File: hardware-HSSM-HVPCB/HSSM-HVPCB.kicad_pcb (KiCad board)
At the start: 2 copper layers, 42 x 36 mm, 66 parts, among them J1 2086-1103, J2 2601-1110, K1 G6DN-1A-L DC12, K2 G6DN-1A-L DC12, Q1 Q_NMOS_SOT-23_IRLML6344, Q2 Q_NMOS_SOT-23_IRLML6344, U1 LNK3204D-TL, U2 CS5480-INZ, U3 LTV-354T, U4 LTV-354T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

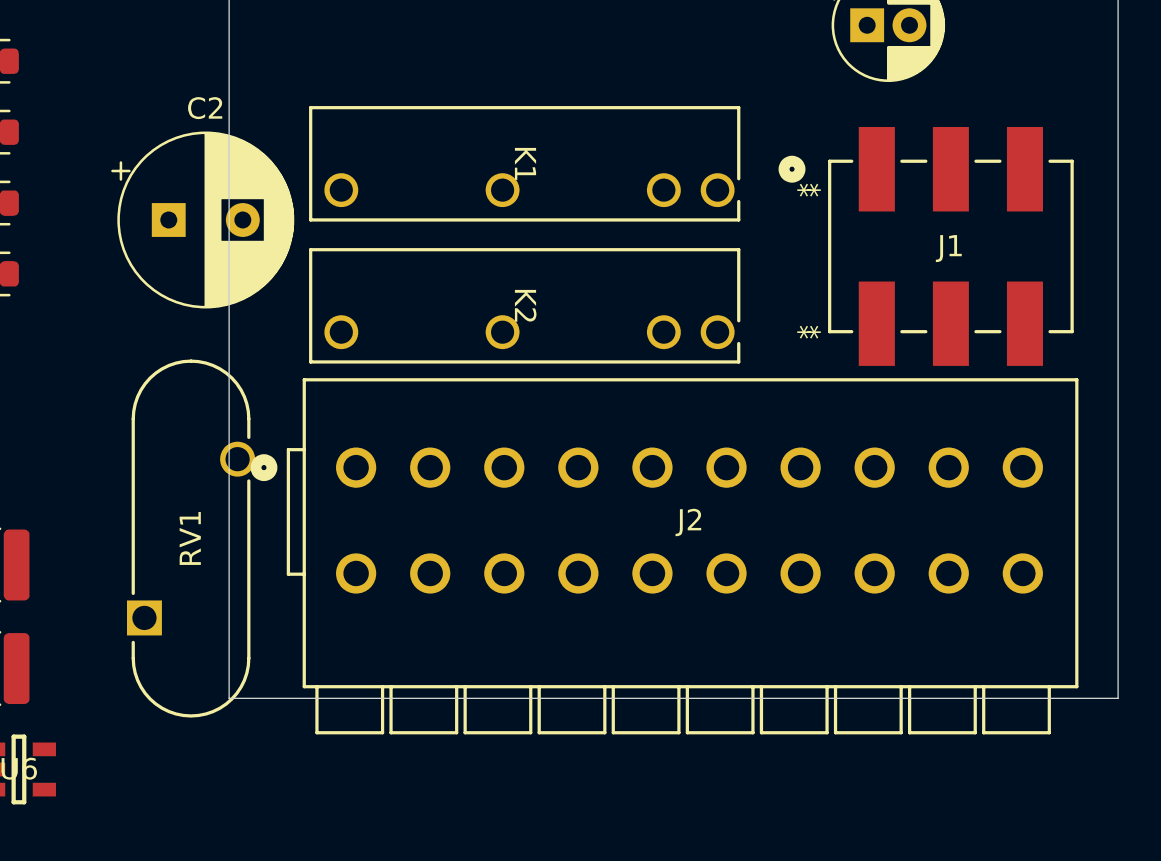
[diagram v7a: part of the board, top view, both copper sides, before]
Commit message: [#6] Replace wago terminal with 8 pos variant
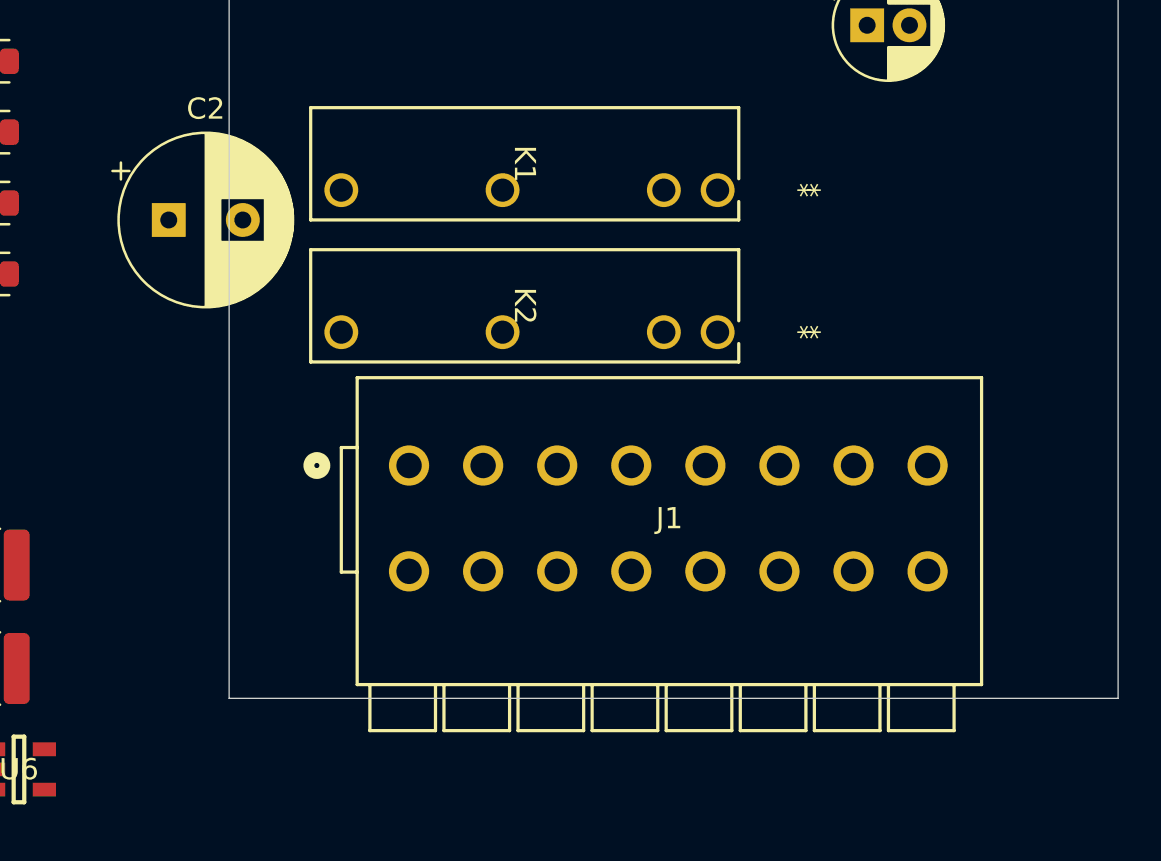
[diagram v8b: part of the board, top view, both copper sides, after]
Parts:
- removed J2: 2601-1110, HSSM-HVPCB:2601-1110
- removed RV1: Varistor_MOV-14D431K, HSSM-HVPCB:MOV-14D431K
- J1: value 2086-1103 -> 2601-1108; footprint HSSM-HVPCB:2086-1103 -> HSSM-HVPCB:2601-1108
- moved J1 27.6 mm to (140.5, 119.0)
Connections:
- J1 pad 1: AC_S2 -> AC_N
- J1 pad 2: AC_S1 -> AC_L
- J1 pad 3: AC_IN -> AC_L
